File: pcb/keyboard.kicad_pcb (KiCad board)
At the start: 2 copper layers, 221 x 100.2 mm, 50 parts, among them J1 TRRS, SW11 Switch, SW12 Switch, SW13 Switch, SW14 Switch, SW15 Switch, SW16 Switch, SW17 Switch, SW18 Switch, SW19 Switch, SW21 Switch, SW22 Switch, SW23 Switch, SW24 Switch, SW25 Switch, SW26 Switch, SW27 Switch, SW28 Switch, SW29 Switch, SW31 Switch, SW32 Switch, SW33 Switch, SW34 Switch, SW35 Switch, SW36 Switch, SW37 Switch, SW38 Switch, SW39 Switch, SW41 Switch, SW42 Switch, SW43 Switch, SW45 Switch, SW46 Switch, SW47 Switch, SW48 Switch, SW49 Switch, U1 EliteC

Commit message: set switch number to silkscreen
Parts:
- JP1, JP2: value JumperSplit -> Jumper
- SW11: value Switch -> 1
- SW12: value Switch -> 2
- SW13: value Switch -> 3
- SW14: value Switch -> 4
- SW15: value Switch -> 5
- SW16: value Switch -> 6
- SW17: value Switch -> 7
- SW18: value Switch -> 8
- SW19: value Switch -> 9
- SW21: value Switch -> 11
- SW22: value Switch -> 12
- SW23: value Switch -> 13
- SW24: value Switch -> 14
- SW25: value Switch -> 15
- SW26: value Switch -> 16
- SW27: value Switch -> 17
- SW28: value Switch -> 18
- SW29: value Switch -> 19
- SW31: value Switch -> 21
- SW32: value Switch -> 22
- SW33: value Switch -> 23
- SW34: value Switch -> 24
- SW35: value Switch -> 25
- SW36: value Switch -> 26
- SW37: value Switch -> 27
- SW38: value Switch -> 28
- SW39: value Switch -> 29
- SW41: value Switch -> 31
- SW42: value Switch -> 32
- SW43: value Switch -> 33
- SW45: value Switch -> 35
- SW46: value Switch -> 36
- SW47: value Switch -> 37
- SW48: value Switch -> 38
- SW49: value Switch -> 39

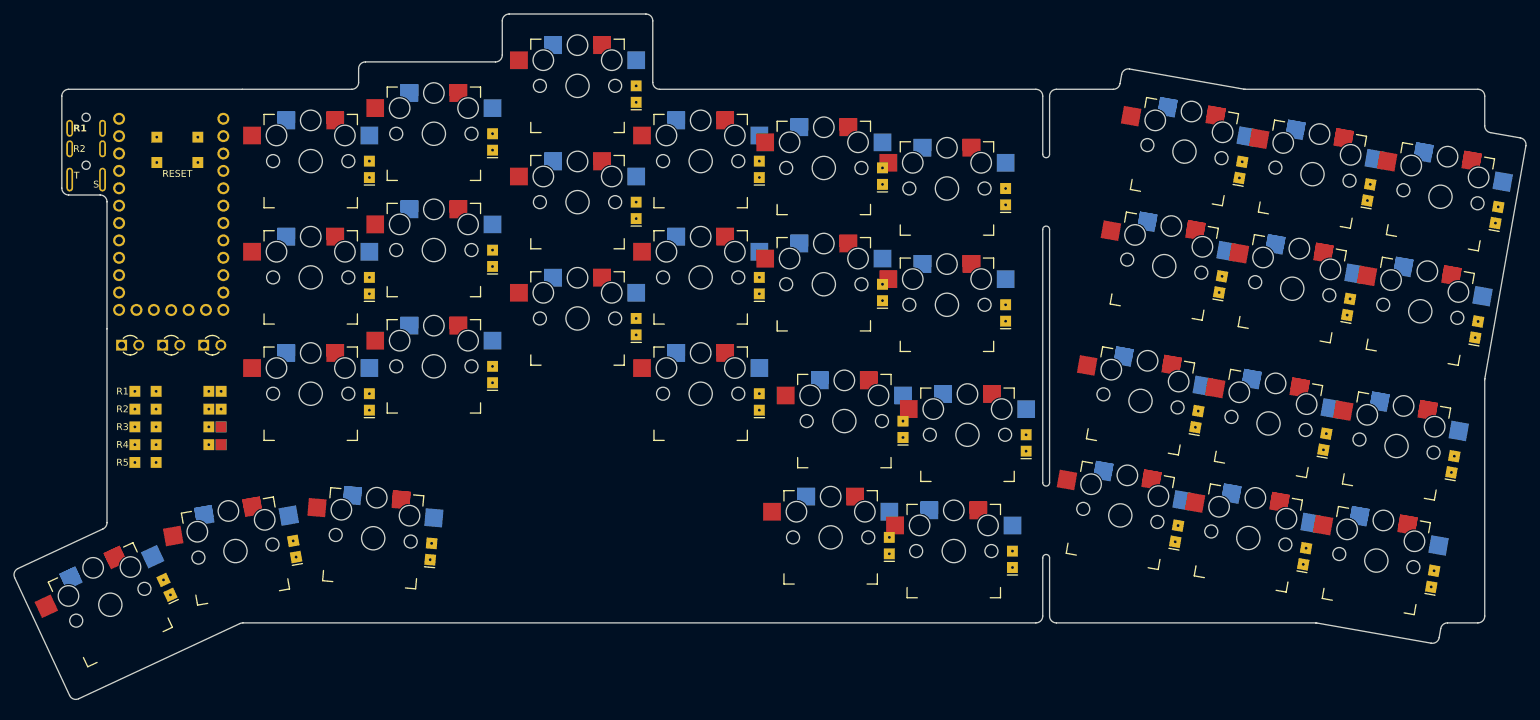
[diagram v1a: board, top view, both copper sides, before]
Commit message: move TRRS to overhang and fix diode positioning
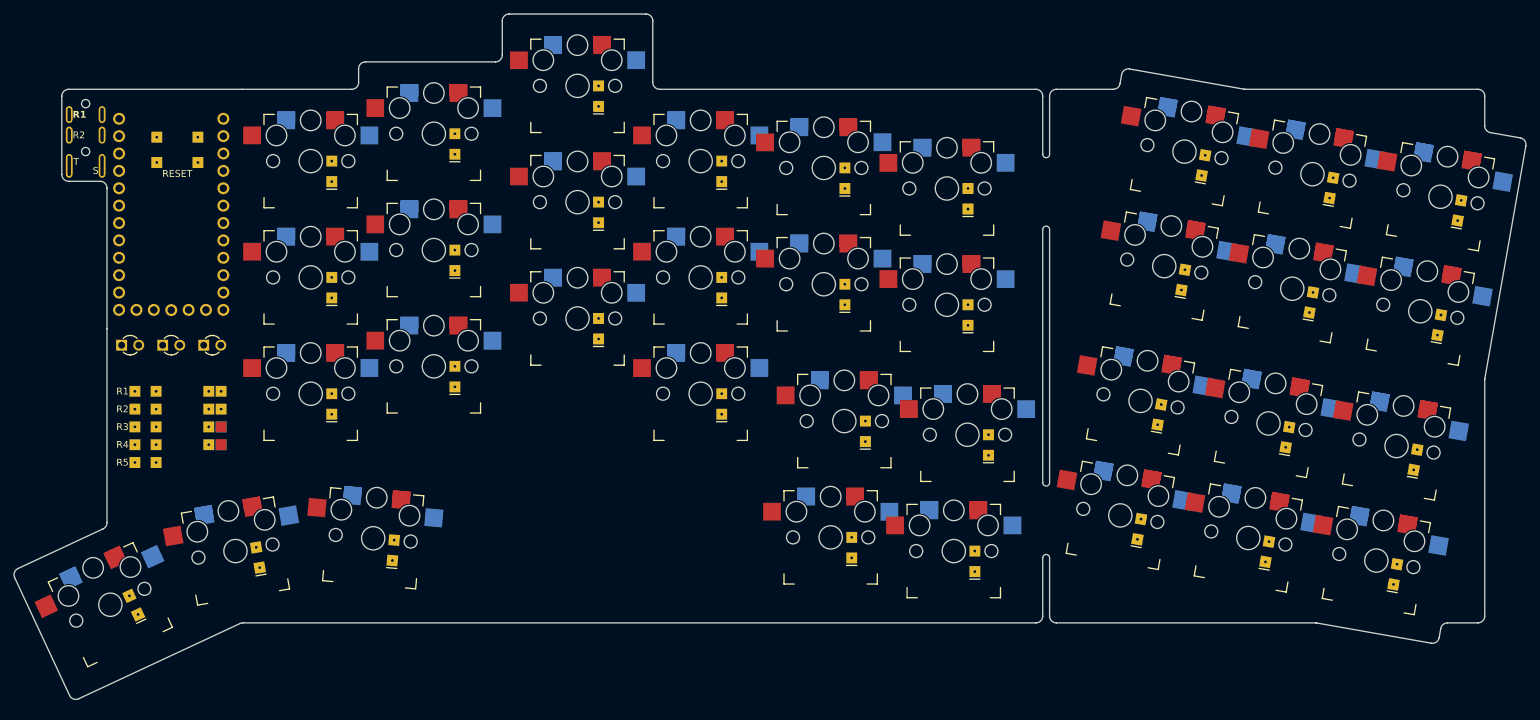
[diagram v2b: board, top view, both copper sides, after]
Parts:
- JP1, JP2: value Jumper -> JumperSplit
- moved J1 0.88 mm to (48.6, 56.2)
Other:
- outline, holes or cut-outs redrawn

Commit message: make adjustments from iteration 11 printout and fix numpad switch positions
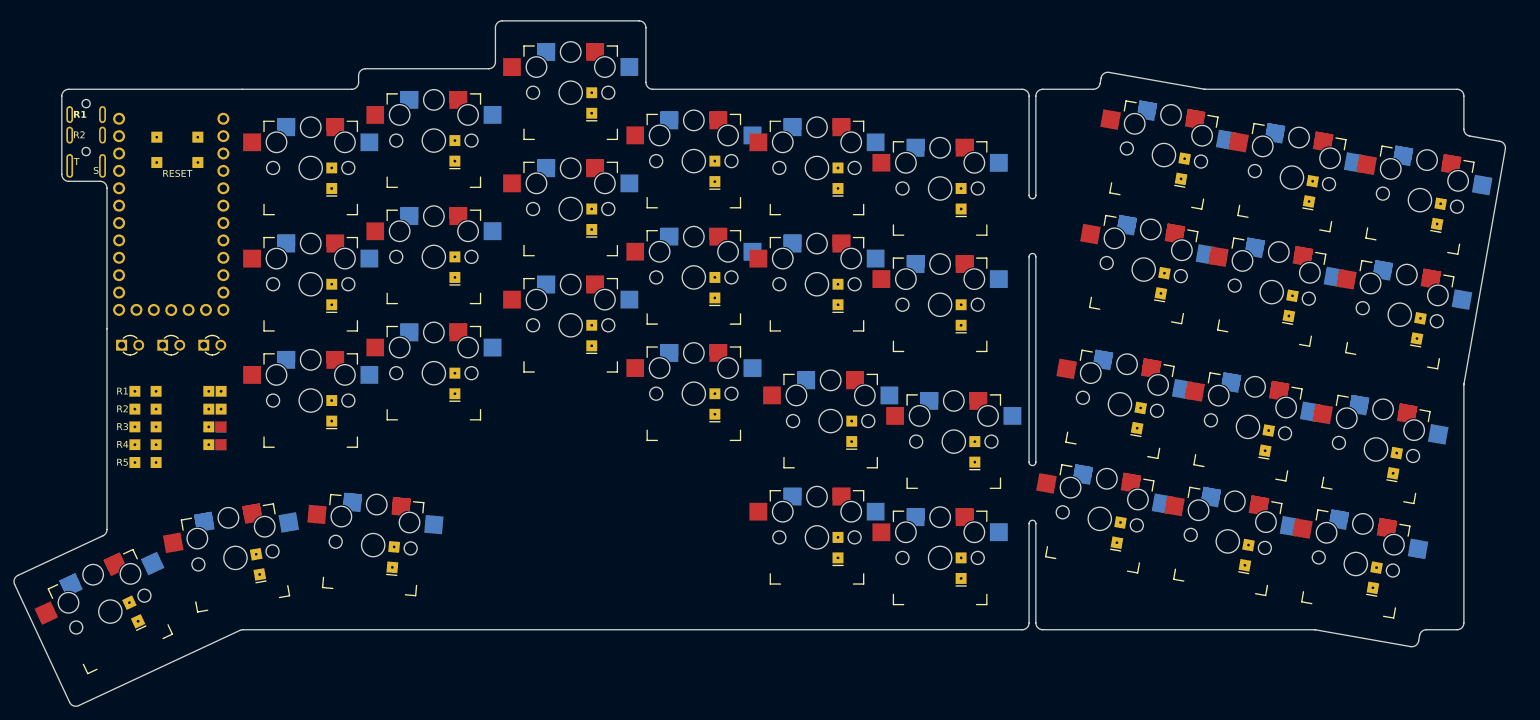
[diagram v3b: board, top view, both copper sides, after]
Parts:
- moved SW17 3.04 mm to (206.2, 59.1)
- moved SW18 3.04 mm to (224.9, 62.4)
- moved SW19 3.04 mm to (243.6, 65.7)
- moved SW27 3.04 mm to (203.3, 75.9)
- moved SW28 3.04 mm to (222.0, 79.2)
- moved SW29 3.04 mm to (240.7, 82.5)
- moved SW37 3.04 mm to (199.8, 95.5)
- moved SW38 3.04 mm to (218.5, 98.8)
- moved SW39 3.04 mm to (237.2, 102.1)
- moved SW47 3.04 mm to (196.8, 112.3)
- moved SW48 3.04 mm to (215.6, 115.6)
- moved SW49 3.04 mm to (234.3, 118.9)
- moved SW36 2.24 mm to (175.5, 101.0)
- moved SW46 2.24 mm to (173.5, 118.0)
- moved SW35 2.00 mm to (157.5, 98.0)
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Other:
- board size 221 x 100.2 mm -> 218 x 100.2 mm

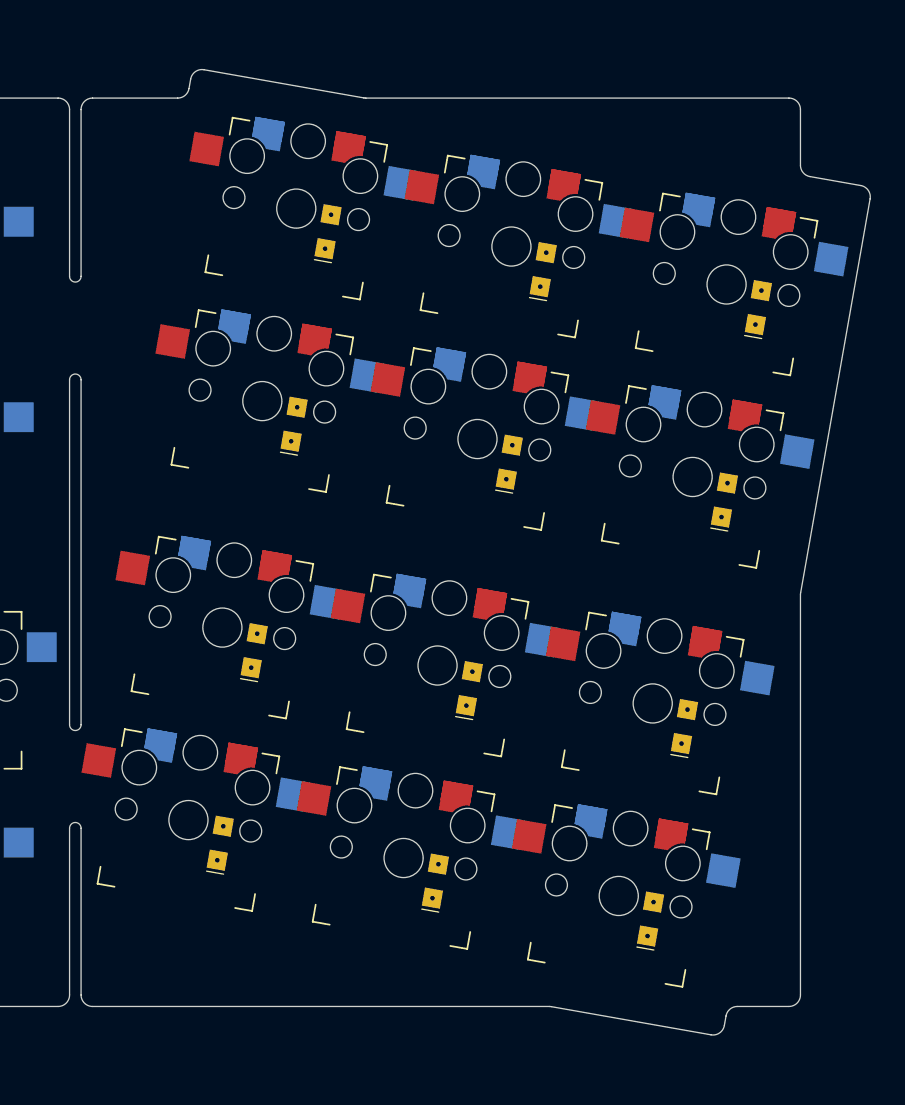
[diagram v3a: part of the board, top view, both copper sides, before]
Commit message: adjust numpad x; add solder mask to jumper; add silkscreen line in snap off
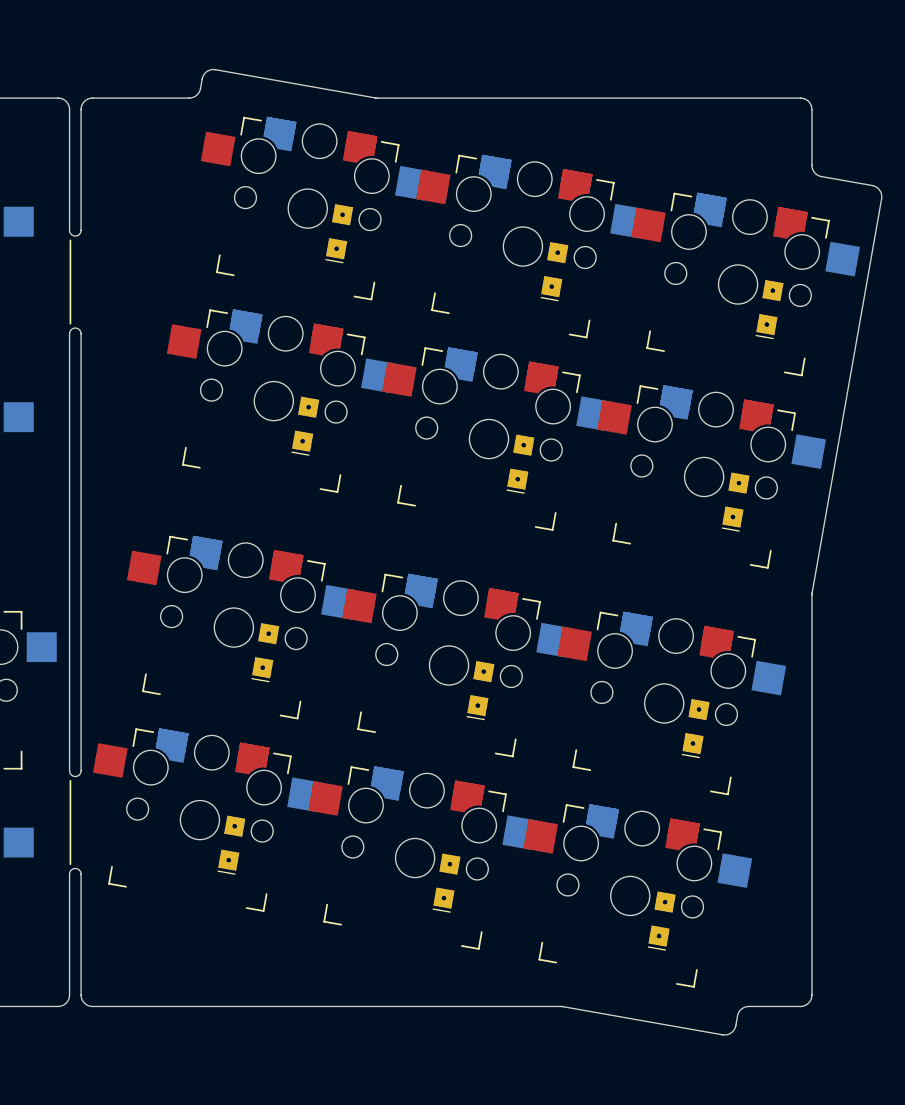
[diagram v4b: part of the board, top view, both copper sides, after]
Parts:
- moved SW17 1.00 mm to (207.2, 59.1)
- moved SW18 1.00 mm to (225.9, 62.4)
- moved SW19 1.00 mm to (244.6, 65.7)
- moved SW27 1.00 mm to (204.3, 75.9)
- moved SW28 1.00 mm to (223.0, 79.2)
- moved SW29 1.00 mm to (241.7, 82.5)
- moved SW37 1.00 mm to (200.8, 95.5)
- moved SW38 1.00 mm to (219.5, 98.8)
- moved SW39 1.00 mm to (238.2, 102.1)
- moved SW47 1.00 mm to (197.8, 112.3)
- moved SW48 1.00 mm to (216.6, 115.6)
- moved SW49 1.00 mm to (235.3, 118.9)
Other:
- board size 218 x 100.2 mm -> 219 x 100.2 mm

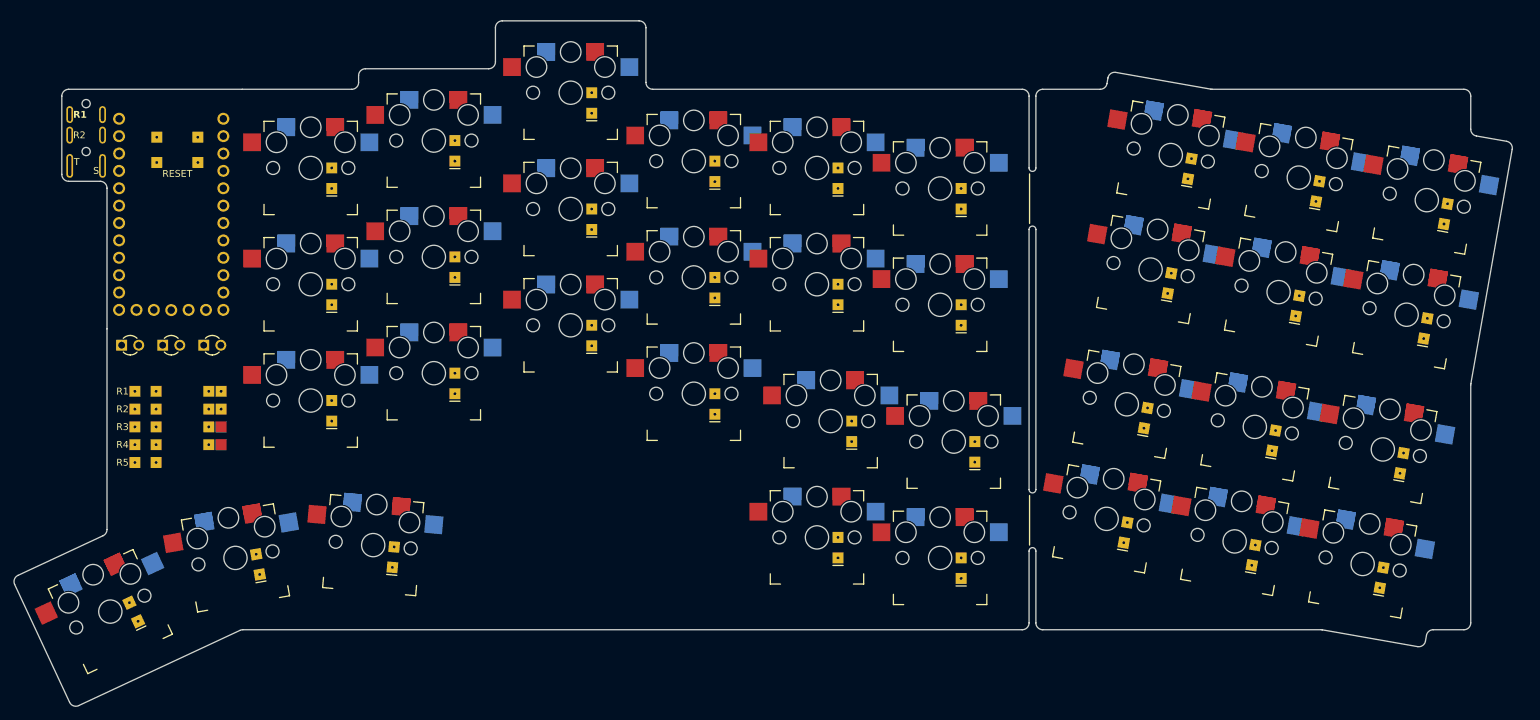
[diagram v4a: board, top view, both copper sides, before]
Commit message: centre snap to switch pads and test traces
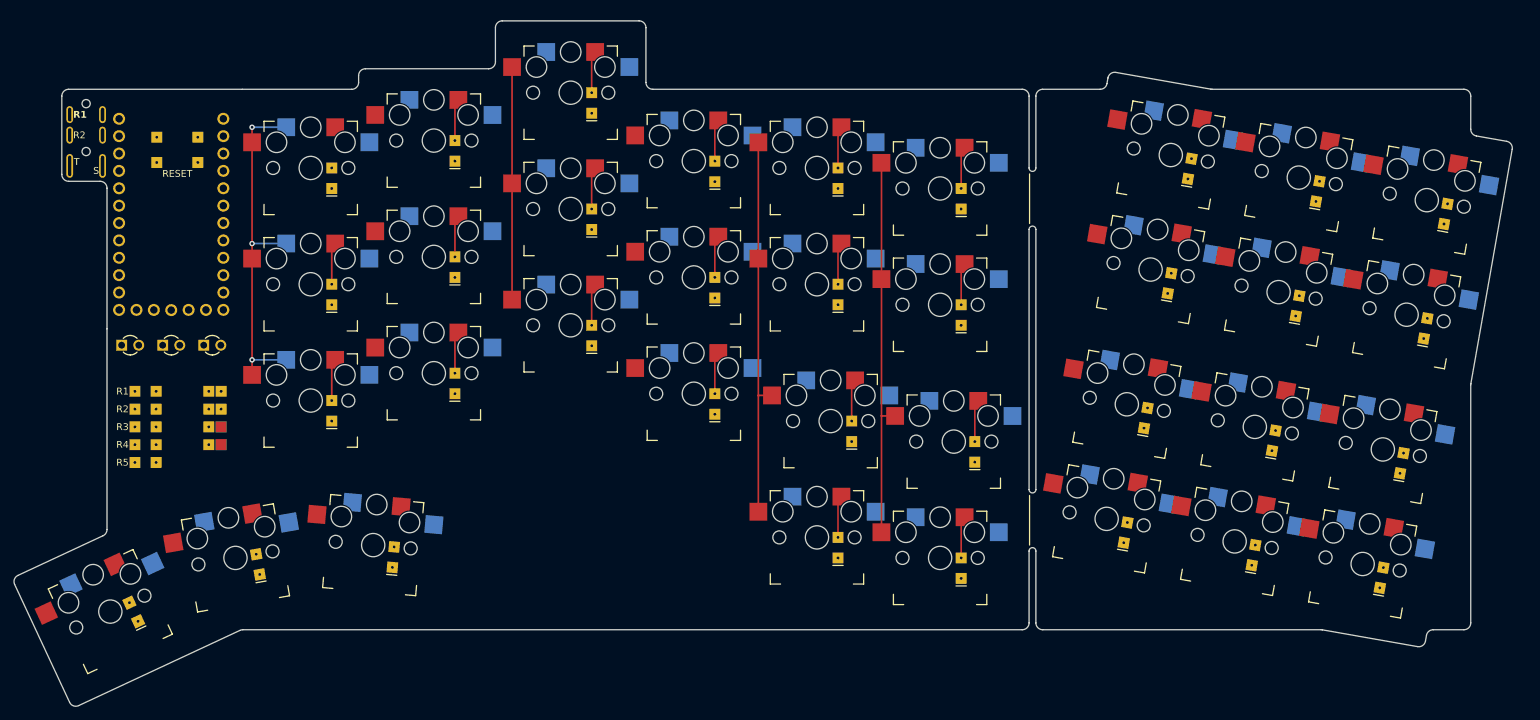
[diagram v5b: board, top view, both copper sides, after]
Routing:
- net COL6: track 0.00 -> 56.0 mm
- net COL5: track 0.00 -> 56.0 mm
- net COL1: track 0.00 -> 51.2 mm, vias 0 -> 3
- net COL3: track 0.00 -> 34.0 mm
- net Net-(SW46-Pad3): track 0.00 -> 6.58 mm
- net Net-(SW45-Pad3): track 0.00 -> 6.58 mm
- net Net-(SW36-Pad3): track 0.00 -> 6.58 mm
- net Net-(SW35-Pad3): track 0.00 -> 6.58 mm
- net Net-(SW34-Pad3): track 0.00 -> 6.58 mm
- net Net-(SW33-Pad3): track 0.00 -> 6.58 mm
- net Net-(SW32-Pad3): track 0.00 -> 6.58 mm
- net Net-(SW31-Pad3): track 0.00 -> 6.58 mm
- net Net-(SW26-Pad3): track 0.00 -> 6.58 mm
- net Net-(SW25-Pad3): track 0.00 -> 6.58 mm
- net Net-(SW24-Pad3): track 0.00 -> 6.58 mm
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
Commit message: experiment with switch label and diode positioning
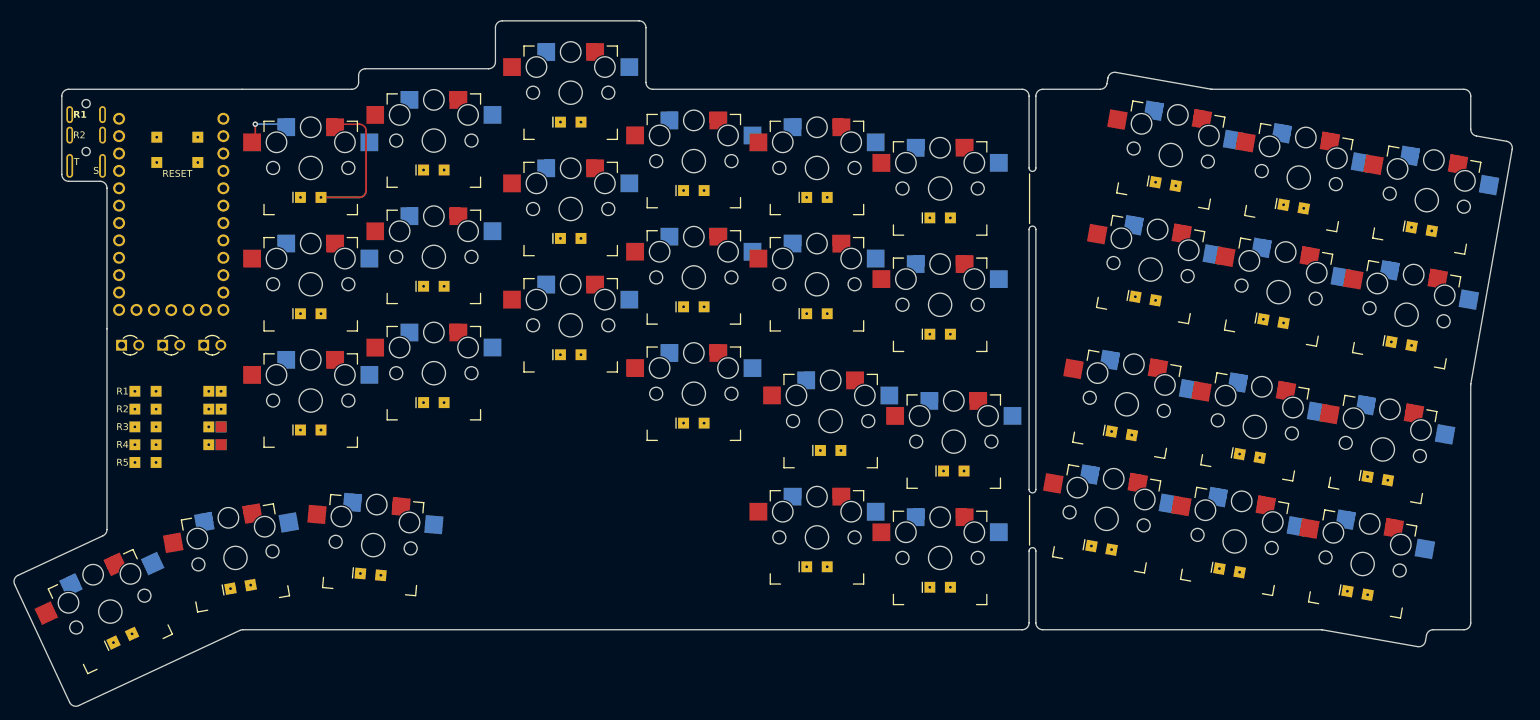
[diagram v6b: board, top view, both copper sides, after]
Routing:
- net COL6: track 56.0 -> 0.00 mm
- net COL5: track 56.0 -> 0.00 mm
- net COL1: track 51.2 -> 8.10 mm, vias 3 -> 1
- net Net-(SW11-Pad3): track 0.00 -> 35.1 mm
- net COL3: track 34.0 -> 0.00 mm
- net Net-(SW46-Pad3): track 6.58 -> 0.00 mm
- net Net-(SW45-Pad3): track 6.58 -> 0.00 mm
- net Net-(SW36-Pad3): track 6.58 -> 0.00 mm
- net Net-(SW35-Pad3): track 6.58 -> 0.00 mm
- net Net-(SW34-Pad3): track 6.58 -> 0.00 mm
- net Net-(SW33-Pad3): track 6.58 -> 0.00 mm
- net Net-(SW32-Pad3): track 6.58 -> 0.00 mm
- net Net-(SW31-Pad3): track 6.58 -> 0.00 mm
- net Net-(SW26-Pad3): track 6.58 -> 0.00 mm
- net Net-(SW25-Pad3): track 6.58 -> 0.00 mm
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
